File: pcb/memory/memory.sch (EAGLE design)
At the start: 19 parts, among them IC1 XMEGA16, IC2 24LC256SN, U1 AS6C1008-55PCN

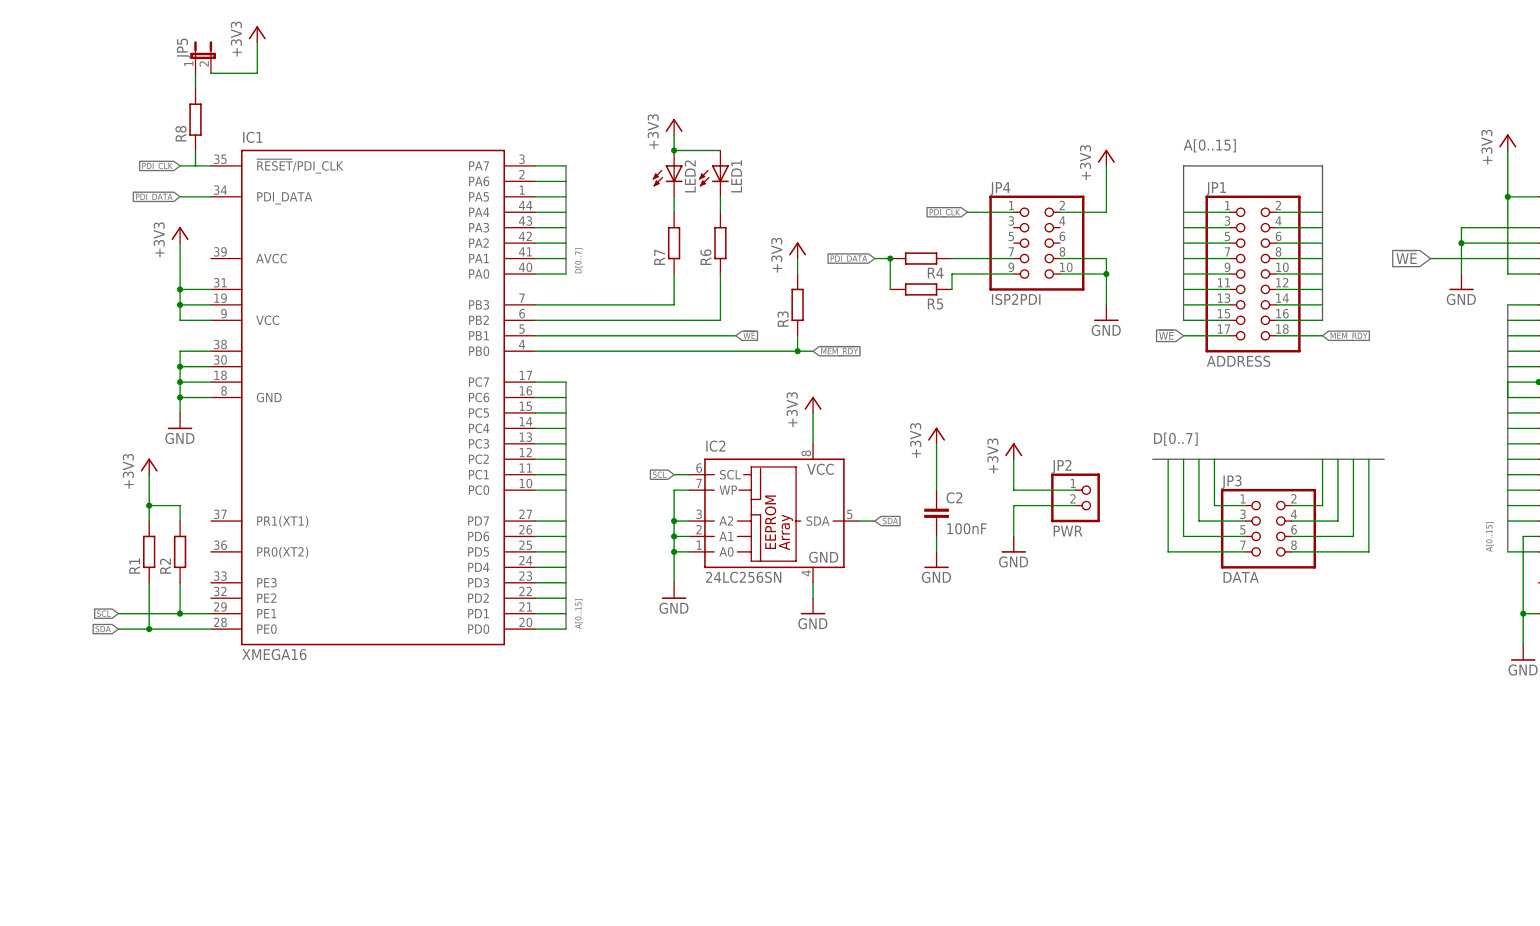
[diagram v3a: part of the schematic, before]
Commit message: Memory board schematic: addeded uart and port reshuffle
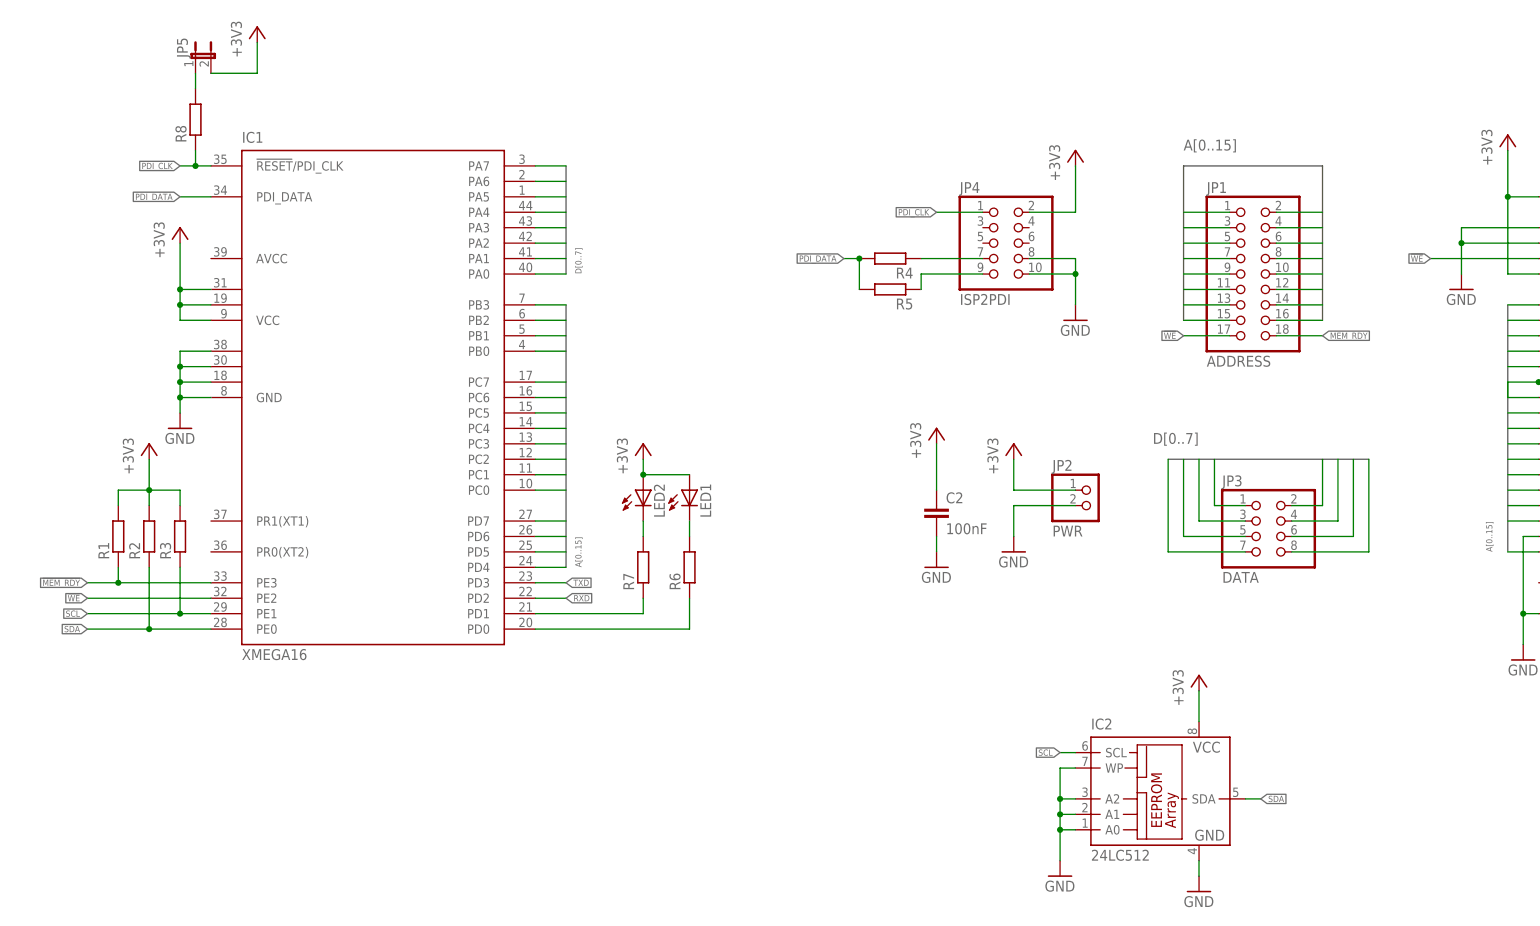
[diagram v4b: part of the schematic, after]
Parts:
- IC2: value 24LC256SN -> 24LC512
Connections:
- new net RXD: IC1.PD2
- new net TXD: IC1.PD3
- net !MEM_RDY!: now also IC1.PE3, R1.1; no longer IC1.PB0, R3.1
- net !WE!: now also IC1.PE2; no longer IC1.PB1
- net A0: now also IC1.PB0; no longer IC1.PD0
- net A1: now also IC1.PB1; no longer IC1.PD1
- net A2: now also IC1.PB2; no longer IC1.PD2
- net A3: now also IC1.PB3; no longer IC1.PD3
- net N$3: now also IC1.PD1, R7.1; no longer IC1.PB2, R6.1
- net N$4: now also IC1.PD0, R6.1; no longer IC1.PB3, R7.1
- net SCL: now also R3.1; no longer R2.1
- net SDA: now also R2.1; no longer R1.1
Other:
- moved on the sheet: IC2, JP4, LED1, LED2, R1, R2, R3, R4, R5, R6, R7
